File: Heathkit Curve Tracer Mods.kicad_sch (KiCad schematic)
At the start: 0 parts

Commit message: updates
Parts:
- added C1: 100, symbol Device:C_Polarized_US
- added C2: 470, Capacitor_SMD:CP_Elec_10x14.3, symbol Device:C_Polarized_US
- added C3: 0.1, Capacitor_SMD:C_0805_2012Metric_Pad1.18x1.45mm_HandSolder, symbol Device:C_US
- added J1: Switch, Connector_PinSocket_2.54mm:PinSocket_1x11_P2.54mm_Vertical, symbol Connector_Generic:Conn_01x11
- added J2: IC6 Jumper, Package_DIP:DIP-14_W10.16mm_LongPads, symbol Connector_Generic:Conn_02x07_Counter_Clockwise
- added J3: +15, Connector_Pin:Pin_D1.3mm_L11.0mm_LooseFit, symbol Connector_Generic:Conn_01x01
- added R1: 10K, Resistor_SMD:R_0805_2012Metric_Pad1.20x1.40mm_HandSolder, symbol Device:R_US
- added R2: 360, symbol Device:R_US
- added S1: (no value), symbol DH_Switches:1P10T
- added U1: 74LS42, Package_SO:SOIC-16W_5.3x10.2mm_P1.27mm, symbol 74xx:74LS42
- added U2: 74LVC1G04, Package_TO_SOT_SMD:SOT-23-5, symbol 74xGxx:74LVC1G04
- added U3: 74LS90, Package_SO:SOIC-14_3.9x8.7mm_P1.27mm, symbol 74xx:74LS90
- added U4: LM7805_TO220, Package_TO_SOT_THT:TO-220-3_Vertical, symbol Regulator_Linear:LM7805_TO220
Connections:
- new net: J2.11 (Pin_11), U1.12 (A3), U3.11 (Q3)
- new net: J2.12 (Pin_12), U1.15 (A0), U3.1 (CP1..3), U3.12 (Q0)
- new net: J2.14 (Pin_14), U3.14 (CP0)
- new net: J2.8 (Pin_8), U1.13 (A2), U3.8 (Q2)
- new net: J2.9 (Pin_9), U1.14 (A1), U3.9 (Q1)
- new net: J3.1 (Pin_1), U4.1 (VI)
- new net: C1.1, R2.2
- new net: U2.4, U3.2 (R0(1))
- new net: J1.8 (Pin_8), U1.10 (8)
- new net: J1.9 (Pin_9), U1.11 (9)
- new net: J1.1 (Pin_1), U1.2 (1)
- new net: J1.2 (Pin_2), U1.3 (2)
- new net: J1.3 (Pin_3), U1.4 (3)
- new net: J1.4 (Pin_4), U1.5 (4)
- new net: J1.5 (Pin_5), U1.6 (5)
- new net: J1.6 (Pin_6), U1.7 (6)
- new net: J1.7 (Pin_7), U1.9 (7)
- new net: J1.11 (Pin_11), R1.1, U2.2
- new net +15V: R2.1
- new net +5V: C2.1, C3.1, J1.10 (Pin_10), J2.5 (Pin_5), U1.16 (VCC), U2.5 (VCC), U3.3 (R0(2)), U3.5 (VCC), U4.3 (VO)
- new net GND: C1.2, C2.2, C3.2, J2.10 (Pin_10), R1.2, U1.8 (GND), U2.3 (GND), U3.10 (GND), U3.6 (R9(1)), U3.7 (R9(2)), U4.2 (GND)
- no-connect marks 0 -> 1
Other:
- removed sheet Logic Supply Update
- removed sheet Sweep Generator Update
- note added: "0 Curves"
- note added: "1 Curves"
- note added: "2 Curves"
- note added: "3 Curves"
- note added: "4 Curves"
- note added: "5 Curves"
- note added: "6 Curves"
- note added: "7 Curves"
- note added: "8 Curves"
- note added: "9 Curves"
- note added: "Mount to chassis"
- note added: "Remove"
- note added: "This circuit replaces the reset logic of the sweep generator by simply plugging into the 74LS90 socket on the PCB. J1 is a 14-pin ribbon cable jumper to that socket. Several additional components on the PCB "should" be removed as they are no longer needed. It should work just fine if they are not removed. Enhancements: 1. The 7.5M potentiometer used in the original circuit is no longer available.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"

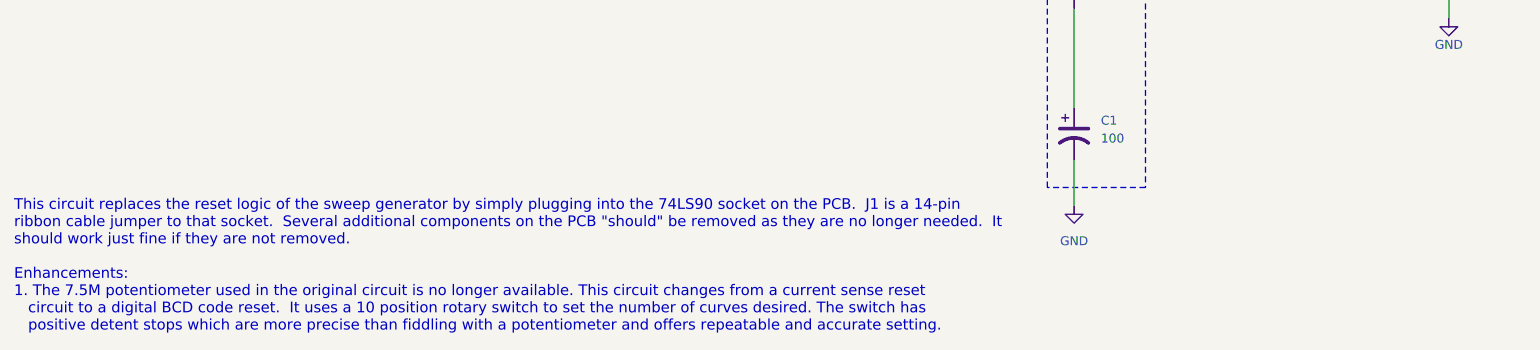
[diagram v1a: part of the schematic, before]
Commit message: updates to schematics, board sent to JLCPCB
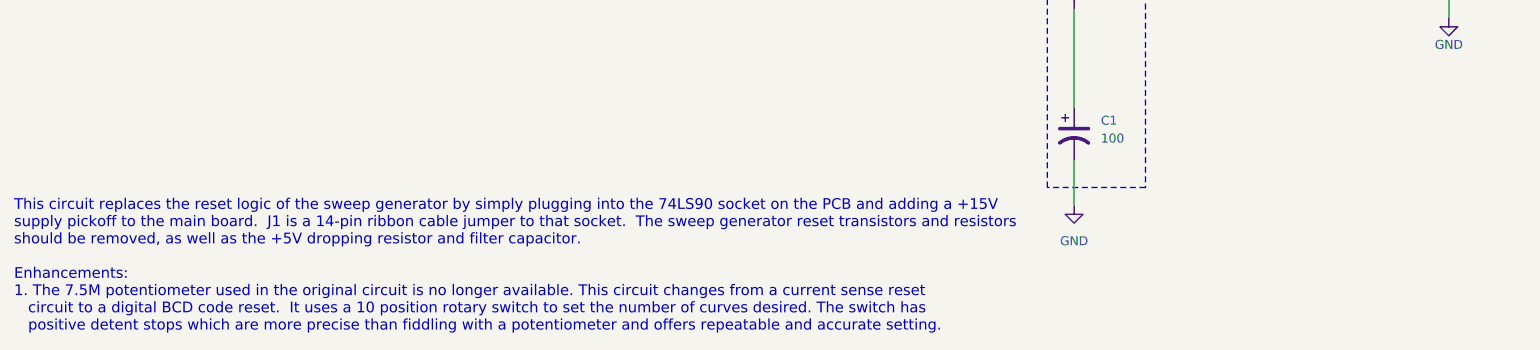
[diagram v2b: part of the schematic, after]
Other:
- note added: "This circuit replaces the reset logic of the sweep generator by simply plugging into the 74LS90 socket on the PCB and adding a +15V supply pickoff to the main board. J1 is a 14-pin ribbon cable jumper to that socket. The sweep generator reset transistors and resistors should be removed, as well as the +5V dropping resistor and filter capacitor. Enhancements: 1. The 7.5M potentiometer used in the 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"
- note removed: "This circuit replaces the reset logic of the sweep generator by simply plugging into the 74LS90 socket on the PCB. J1 is a 14-pin ribbon cable jumper to that socket. Several additional components on the PCB "should" be removed as they are no longer needed. It should work just fine if they are not removed. Enhancements: 1. The 7.5M potentiometer used in the original circuit is no longer available.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"
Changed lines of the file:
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@@
 		)
 	)
-	(text "This circuit replaces the reset logic of the sweep generator by simply plugging into the 74LS90 socket on the PCB.  J1 is a 14-pin \nribbon cable jumper to that socket.  Several additional components on the PCB \"should\" be removed as they are no longer needed.  It \nshould work just fine if they are not removed.\n\nEnhancements:\n1. The 7.5M potentiometer used in the original circuit is no longer available. This circuit changes from a current sense reset \n   circuit to a digital BCD code reset.  It uses a 10 position rotary switch to set the number of curves desired. The switch has \n   positive detent stops which are more precise than fiddling with a potentiometer and offers repeatable and accurate setting. \n"
+	(text "This circuit replaces the reset logic of the sweep generator by simply plugging into the 74LS90 socket on the PCB and adding a +15V\nsupply pickoff to the main board.  J1 is a 14-pin ribbon cable jumper to that socket.  The sweep generator reset transistors and resistors\nshould be removed, as well as the +5V dropping resistor and filter capacitor.\n\nEnhancements:\n1. The 7.5M potentiometer used in the original circuit is no longer available. This circuit changes from a current sense reset \n   circuit to a digital BCD code reset.  It uses a 10 position rotary switch to set the number of curves desired. The switch has \n   positive detent stops which are more precise than fiddling with a potentiometer and offers repeatable and accurate setting. \n"
 		(exclude_from_sim no)
 		(at 25.654 147.066 0)

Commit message: Documentation
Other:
- title: (none) -> Heathkit IT-x121 Curve Tracer Modifications
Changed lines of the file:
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@@
 	(generator "eeschema")
 	(generator_version "10.0")
-	(paper "A4")
+	(paper "USLetter")
+	(title_block
+		(title "Heathkit IT-x121 Curve Tracer Modifications")
+		(date "2026-07-22")
+		(rev "B")
+	)
 	(rectangle
 		(start 172.72 102.87)

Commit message: updates after testing
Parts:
- J2: footprint Package_DIP:DIP-14_W10.16mm_LongPads -> Package_DIP:DIP-14_W7.62mm_LongPads
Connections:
- net +5V: now also J1.2 (Pin_2); no longer J1.10 (Pin_10)
- net at U1.10 (8): now also J1.4 (Pin_4); no longer J1.8 (Pin_8)
- net at U1.11 (9): now also J1.3 (Pin_3); no longer J1.9 (Pin_9)
- net at U1.2 (1): now also J1.11 (Pin_11); no longer J1.1 (Pin_1)
- net at U1.3 (2): now also J1.10 (Pin_10); no longer J1.2 (Pin_2)
- net at U1.4 (3): now also J1.9 (Pin_9); no longer J1.3 (Pin_3)
- net at U1.5 (4): now also J1.8 (Pin_8); no longer J1.4 (Pin_4)
- net at U1.6 (5): now also J1.7 (Pin_7); no longer J1.5 (Pin_5)
- net at U1.9 (7): now also J1.5 (Pin_5); no longer J1.7 (Pin_7)
- net at R1.1, U2.2: now also J1.1 (Pin_1); no longer J1.11 (Pin_11)
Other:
- moved on the sheet: J1
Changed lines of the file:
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@@
 	(text "This circuit replaces the reset logic of the sweep generator by simply plugging into the 74LS90 socket on the PCB and adding a +15V\nsupply pickoff to the main board.  J1 is a 14-pin ribbon cable jumper to that socket.  The sweep generator reset transistors and resistors\nshould be removed, as well as the +5V dropping resistor and filter capacitor.\n\nEnhancements:\n1. The 7.5M potentiometer used in the original circuit is no longer available. This circuit changes from a current sense reset \n   circuit to a digital BCD code reset.  It uses a 10 position rotary switch to set the number of curves desired. The switch has \n   positive detent stops which are more precise than fiddling with a potentiometer and offers repeatable and accurate setting. \n"
 		(exclude_from_sim no)
-		(at 25.654 147.066 0)
+		(at 25.146 158.496 0)
 		(effects
 			(font
@@
 	(wire
 		(pts
-			(xy 71.12 74.93) (xy 86.36 74.93)
+			(xy 182.88 74.93) (xy 177.8 74.93)
 		)
 		(stroke
@@
 	(wire
 		(pts
-			(xy 182.88 74.93) (xy 177.8 74.93)
+			(xy 99.06 82.55) (xy 99.06 85.09)
 		)
 		(stroke
@@
 	(wire
 		(pts
-			(xy 99.06 82.55) (xy 99.06 85.09)
+			(xy 241.3 55.88) (xy 241.3 62.23)
 		)
 		(stroke
@@
 	(wire
 		(pts
-			(xy 241.3 55.88) (xy 241.3 62.23)
+			(xy 208.28 72.39) (xy 208.28 27.94)
 		)
 		(stroke
@@
 	(wire
 		(pts
-			(xy 208.28 72.39) (xy 208.28 27.94)
+			(xy 54.61 74.93) (xy 63.5 74.93)
 		)
 		(stroke
@@
 	(wire
 		(pts
-			(xy 54.61 74.93) (xy 63.5 74.93)
+			(xy 74.93 90.17) (xy 74.93 93.98)
 		)
 		(stroke
@@
 	(wire
 		(pts
-			(xy 74.93 90.17) (xy 74.93 93.98)
+			(xy 111.76 54.61) (xy 125.73 54.61)
 		)
 		(stroke
@@
 	(wire
 		(pts
-			(xy 111.76 54.61) (xy 125.73 54.61)
+			(xy 71.12 59.69) (xy 86.36 59.69)
 		)
 		(stroke
@@
 	(wire
 		(pts
-			(xy 195.58 64.77) (xy 198.12 64.77)
+			(xy 71.12 57.15) (xy 86.36 57.15)
 		)
 		(stroke
@@
 	(wire
 		(pts
-			(xy 38.1 80.01) (xy 63.5 80.01)
+			(xy 195.58 64.77) (xy 198.12 64.77)
 		)
 		(stroke
@@
 	(wire
 		(pts
-			(xy 214.63 100.33) (xy 222.25 100.33)
+			(xy 38.1 80.01) (xy 63.5 80.01)
 		)
 		(stroke
@@
 	(wire
 		(pts
-			(xy 116.84 78.74) (xy 116.84 80.01)
+			(xy 214.63 100.33) (xy 222.25 100.33)
 		)
 		(stroke
@@
 	(wire
 		(pts
-			(xy 71.12 80.01) (xy 74.93 80.01)
+			(xy 116.84 78.74) (xy 116.84 80.01)
 		)
 		(stroke
@@
 	(wire
 		(pts
-			(xy 71.12 57.15) (xy 86.36 57.15)
+			(xy 71.12 67.31) (xy 86.36 67.31)
 		)
 		(stroke
@@
 	(wire
 		(pts
+			(xy 71.12 54.61) (xy 86.36 54.61)
+		)
+		(stroke
+			(width 0)
+			(type default)
+		)
+	)
+	(wire
+		(pts
+			(xy 71.12 69.85) (xy 86.36 69.85)
+		)
+		(stroke
+			(width 0)
+			(type default)
+		)
+	)
+	(wire
+		(pts
 			(xy 195.58 77.47) (xy 203.2 77.47)
 		)
@@
 	(wire
 		(pts
-			(xy 71.12 54.61) (xy 86.36 54.61)
-		)
-		(stroke
-			(width 0)
-			(type default)
-		)
-	)
-	(wire
-		(pts
 			(xy 111.76 59.69) (xy 120.65 59.69)
 		)
@@
 	(wire
 		(pts
-			(xy 231.14 50.8) (xy 231.14 55.88)
+			(xy 71.12 64.77) (xy 86.36 64.77)
 		)
 		(stroke
@@
 	(wire
 		(pts
-			(xy 123.19 57.15) (xy 129.54 57.15)
+			(xy 231.14 50.8) (xy 231.14 55.88)
 		)
 		(stroke
@@
 	(wire
 		(pts
-			(xy 71.12 64.77) (xy 86.36 64.77)
+			(xy 123.19 57.15) (xy 129.54 57.15)
 		)
 		(stroke
@@
 	(wire
 		(pts
-			(xy 71.12 62.23) (xy 86.36 62.23)
-		)
-		(stroke
-			(width 0)
-			(type default)
-		)
-	)
-	(wire
-		(pts
 			(xy 198.12 74.93) (xy 195.58 74.93)
 		)
@@
 	(wire
 		(pts
-			(xy 71.12 72.39) (xy 86.36 72.39)
+			(xy 54.61 67.31) (xy 63.5 67.31)
 		)
 		(stroke
@@
 	(wire
 		(pts
-			(xy 54.61 67.31) (xy 63.5 67.31)
+			(xy 99.06 41.91) (xy 99.06 44.45)
 		)
 		(stroke
@@
 	(wire
 		(pts
-			(xy 99.06 41.91) (xy 99.06 44.45)
+			(xy 157.48 78.74) (xy 142.24 78.74)
 		)
 		(stroke
@@
 	(wire
 		(pts
-			(xy 157.48 78.74) (xy 142.24 78.74)
+			(xy 176.53 110.49) (xy 176.53 124.46)
 		)
 		(stroke
@@
 	(wire
 		(pts
-			(xy 176.53 110.49) (xy 176.53 124.46)
+			(xy 154.94 69.85) (xy 157.48 69.85)
 		)
 		(stroke
@@
 	(wire
 		(pts
-			(xy 154.94 69.85) (xy 157.48 69.85)
+			(xy 74.93 80.01) (xy 74.93 90.17)
 		)
 		(stroke
@@
 	(wire
 		(pts
-			(xy 71.12 59.69) (xy 86.36 59.69)
+			(xy 160.02 90.17) (xy 160.02 59.69)
 		)
 		(stroke
@@
 	(wire
 		(pts
-			(xy 74.93 80.01) (xy 74.93 90.17)
+			(xy 157.48 67.31) (xy 157.48 69.85)
 		)
 		(stroke
@@
 	(wire
 		(pts
-			(xy 160.02 90.17) (xy 160.02 59.69)
+			(xy 128.27 35.56) (xy 128.27 43.18)
 		)
 		(stroke
@@
 	(wire
 		(pts
-			(xy 157.48 67.31) (xy 157.48 69.85)
+			(xy 71.12 80.01) (xy 74.93 80.01)
 		)
 		(stroke
@@
 	(wire
 		(pts
-			(xy 128.27 35.56) (xy 128.27 43.18)
+			(xy 176.53 96.52) (xy 176.53 100.33)
 		)
 		(stroke
@@
 	(wire
 		(pts
-			(xy 176.53 96.52) (xy 176.53 100.33)
+			(xy 195.58 80.01) (xy 205.74 80.01)
 		)
 		(stroke
@@
 	(wire
 		(pts
-			(xy 71.12 69.85) (xy 86.36 69.85)
+			(xy 71.12 72.39) (xy 86.36 72.39)
 		)
 		(stroke
@@
 	(wire
 		(pts
-			(xy 195.58 80.01) (xy 205.74 80.01)
+			(xy 71.12 77.47) (xy 74.93 77.47)
 		)
 		(stroke
@@
 	(wire
 		(pts
-			(xy 71.12 67.31) (xy 86.36 67.31)
+			(xy 203.2 33.02) (xy 125.73 33.02)
 		)
 		(stroke
@@
 	(wire
 		(pts
-			(xy 203.2 33.02) (xy 125.73 33.02)
+			(xy 71.12 62.23) (xy 86.36 62.23)
 		)
 		(stroke
@@
 	(wire
 		(pts
-			(xy 54.61 57.15) (xy 63.5 57.15)
+			(xy 71.12 74.93) (xy 86.36 74.93)
 		)
 		(stroke
@@
 	(wire
 		(pts
-			(xy 142.24 78.74) (xy 142.24 80.01)
+			(xy 54.61 57.15) (xy 63.5 57.15)
 		)
 		(stroke
@@
 	(wire
 		(pts
-			(xy 142.24 77.47) (xy 142.24 78.74)
+			(xy 142.24 78.74) (xy 142.24 80.01)
 		)
 		(stroke
@@
 	(wire
 		(pts
-			(xy 74.93 77.47) (xy 71.12 77.47)
+			(xy 142.24 77.47) (xy 142.24 78.74)
 		)
 		(stroke
@@
 			)
 		)
-		(property "Footprint" "Package_DIP:DIP-14_W10.16mm_LongPads"
+		(property "Footprint" "Package_DIP:DIP-14_W7.62mm_LongPads"
 			(at 187.96 72.39 0)
 			(hide yes)
@@
 	(symbol
 		(lib_id "Connector_Generic:Conn_01x11")
-		(at 66.04 67.31 0)
-		(mirror y)
+		(at 66.04 67.31 180)
 		(unit 1)
 		(body_style 1)
@@
 		(dnp no)
 		(property "Reference" "J1"
-			(at 66.04 86.36 0)
+			(at 66.04 48.26 0)
 			(show_name no)
 			(do_not_autoplace no)
@@
 		)
 		(property "Value" "Switch"
-			(at 66.04 83.82 0)
+			(at 66.04 50.8 0)
 			(show_name no)
 			(do_not_autoplace no)

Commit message: updates
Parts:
- removed J3: +15, Connector_Pin:Pin_D1.3mm_L11.0mm_LooseFit, symbol Connector_Generic:Conn_01x01
- removed U2: 74LVC1G04, Package_TO_SOT_SMD:SOT-23-5, symbol 74xGxx:74LVC1G04
- added Q1: 2N3904, Package_TO_SOT_THT:TO-92L_HandSolder, symbol Transistor_BJT:2N3904
- added R1: 1K, Resistor_THT:R_Axial_DIN0207_L6.3mm_D2.5mm_P7.62mm_Horizontal, symbol Device:R_US
- added R3: 10K, Resistor_THT:R_Axial_DIN0207_L6.3mm_D2.5mm_P7.62mm_Horizontal, symbol Device:R_US
- C2: footprint Capacitor_SMD:CP_Elec_10x14.3 -> Capacitor_THT:CP_Radial_D10.0mm_P3.80mm
- C3: footprint Capacitor_SMD:C_0805_2012Metric_Pad1.18x1.45mm_HandSolder -> Capacitor_THT:C_Disc_D4.7mm_W2.5mm_P5.00mm
- J2: footprint Package_DIP:DIP-14_W7.62mm_LongPads -> Package_DIP:DIP-14_W7.62mm_Socket_LongPads
- R2: renamed from R1; footprint Resistor_SMD:R_0805_2012Metric_Pad1.20x1.40mm_HandSolder -> Resistor_THT:R_Axial_DIN0207_L6.3mm_D2.5mm_P7.62mm_Horizontal
- U1: footprint Package_SO:SOIC-16W_5.3x10.2mm_P1.27mm -> Package_DIP:DIP-16_W7.62mm_Socket_LongPads
- U2: renamed from U3; footprint Package_SO:SOIC-14_3.9x8.7mm_P1.27mm -> Package_DIP:DIP-14_W7.62mm_Socket_LongPads
- renumbered R2 to R4, U4 to U3
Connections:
- net +15V: now also U3.1 (VI)
- net +5V: now also J1.11 (Pin_11), R3.1; no longer J1.2 (Pin_2), U3.3 (VO)
- net GND: now also J2.6 (Pin_6), Q1.1 (E)
- net at J2.2 (Pin_2): now also U2.2 (R0(1)), Q1.3 (C), R3.2
- net at C1.1, R4.2: now also U3.3 (VO)
- net at U1.10 (8): now also J1.9 (Pin_9); no longer J1.4 (Pin_4)
- net at U1.11 (9): now also J1.10 (Pin_10); no longer J1.3 (Pin_3)
- net at U1.2 (1): now also J1.2 (Pin_2); no longer J1.11 (Pin_11)
- net at U1.3 (2): now also J1.3 (Pin_3); no longer J1.10 (Pin_10)
- net at U1.4 (3): now also J1.4 (Pin_4); no longer J1.9 (Pin_9)
- net at U1.5 (4): now also J1.5 (Pin_5); no longer J1.8 (Pin_8)
- net at U1.6 (5): now also J1.6 (Pin_6); no longer J1.7 (Pin_7)
- net at U1.7 (6): now also J1.7 (Pin_7); no longer J1.6 (Pin_6)
- net at U1.9 (7): now also J1.8 (Pin_8); no longer J1.5 (Pin_5)
- net at R2.1: now also Q1.2 (B), R1.2; no longer J1.1 (Pin_1)
- new net: J1.1 (Pin_1), R1.1
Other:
- moved on the sheet: C1, J1, J2, R2, R4, U3
